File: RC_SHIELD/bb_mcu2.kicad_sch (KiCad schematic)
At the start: 14 parts, among them J1 SWD, J2 P3a, SW301 SW_Push, U1 STM32F030K6Tx, Y1 8MHz

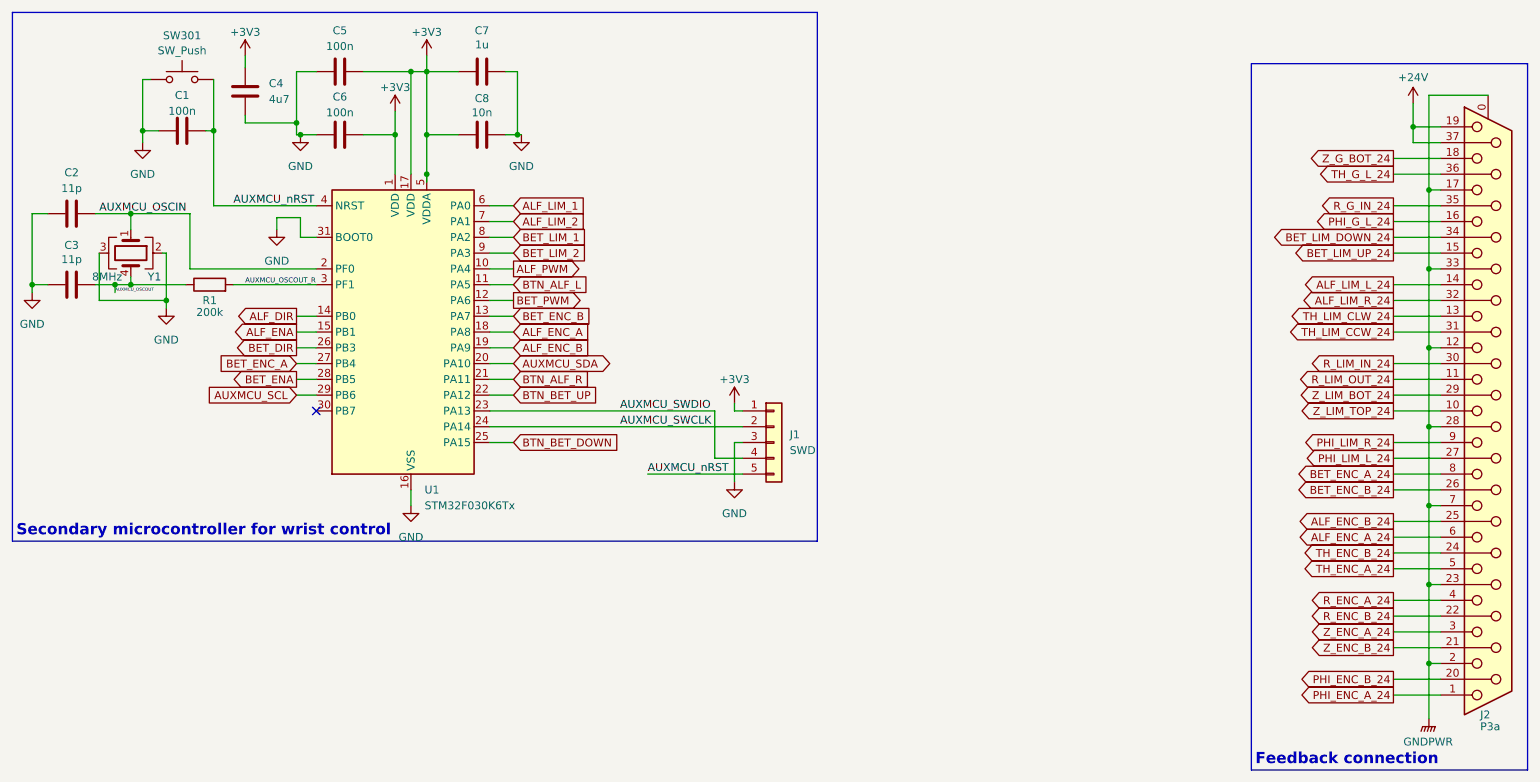
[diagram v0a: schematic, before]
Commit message: Revert "[SCH] reannotated entire schematic so PCBnew wont complain"
This reverts commit df148950bb8496d2d5af5a937770664cb0004a0d.
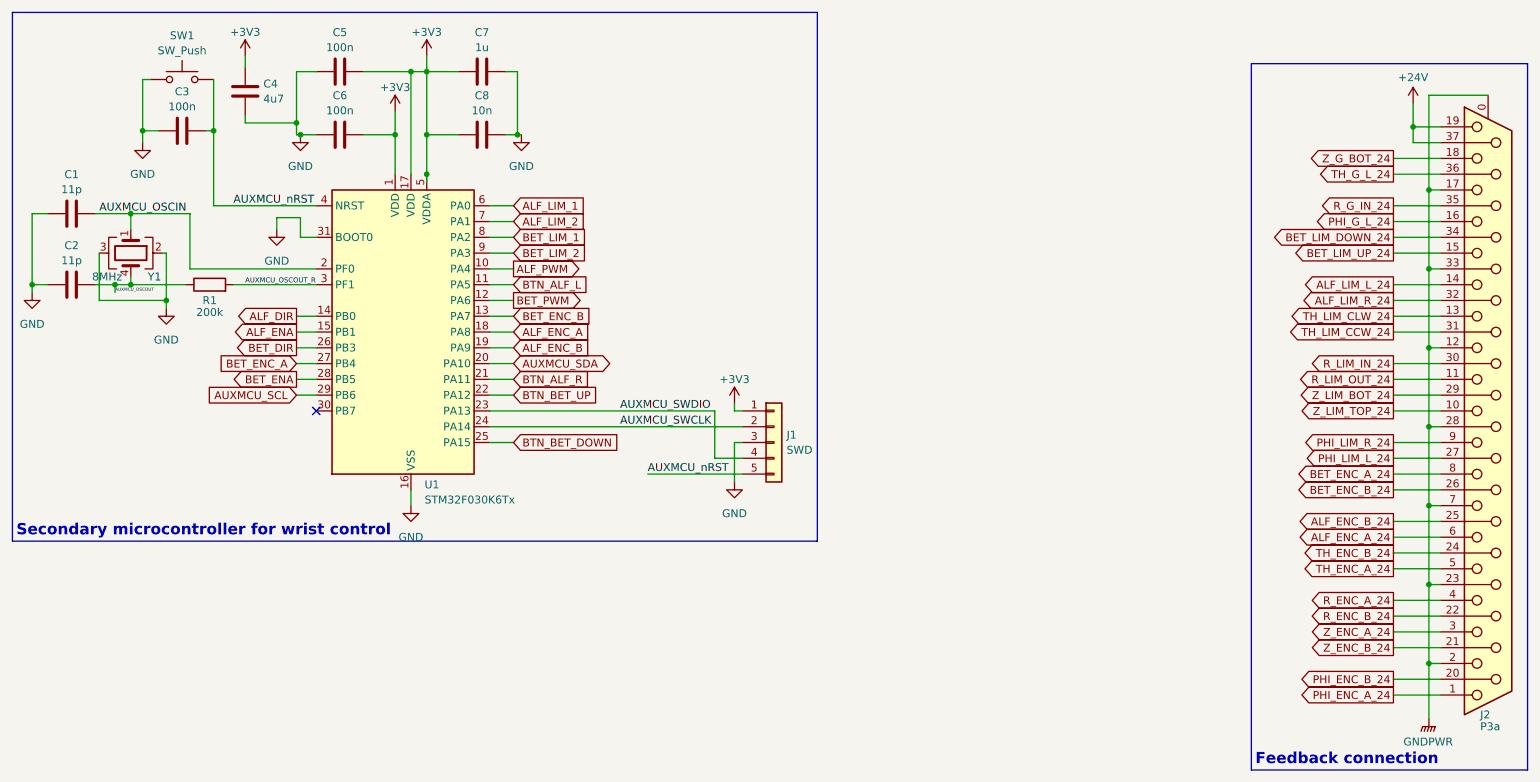
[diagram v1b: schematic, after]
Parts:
- renumbered C2 to C1, C3 to C2, C1 to C3, SW301 to SW1

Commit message: [SCH] reannotated entire schematic so PCBnew wont complain
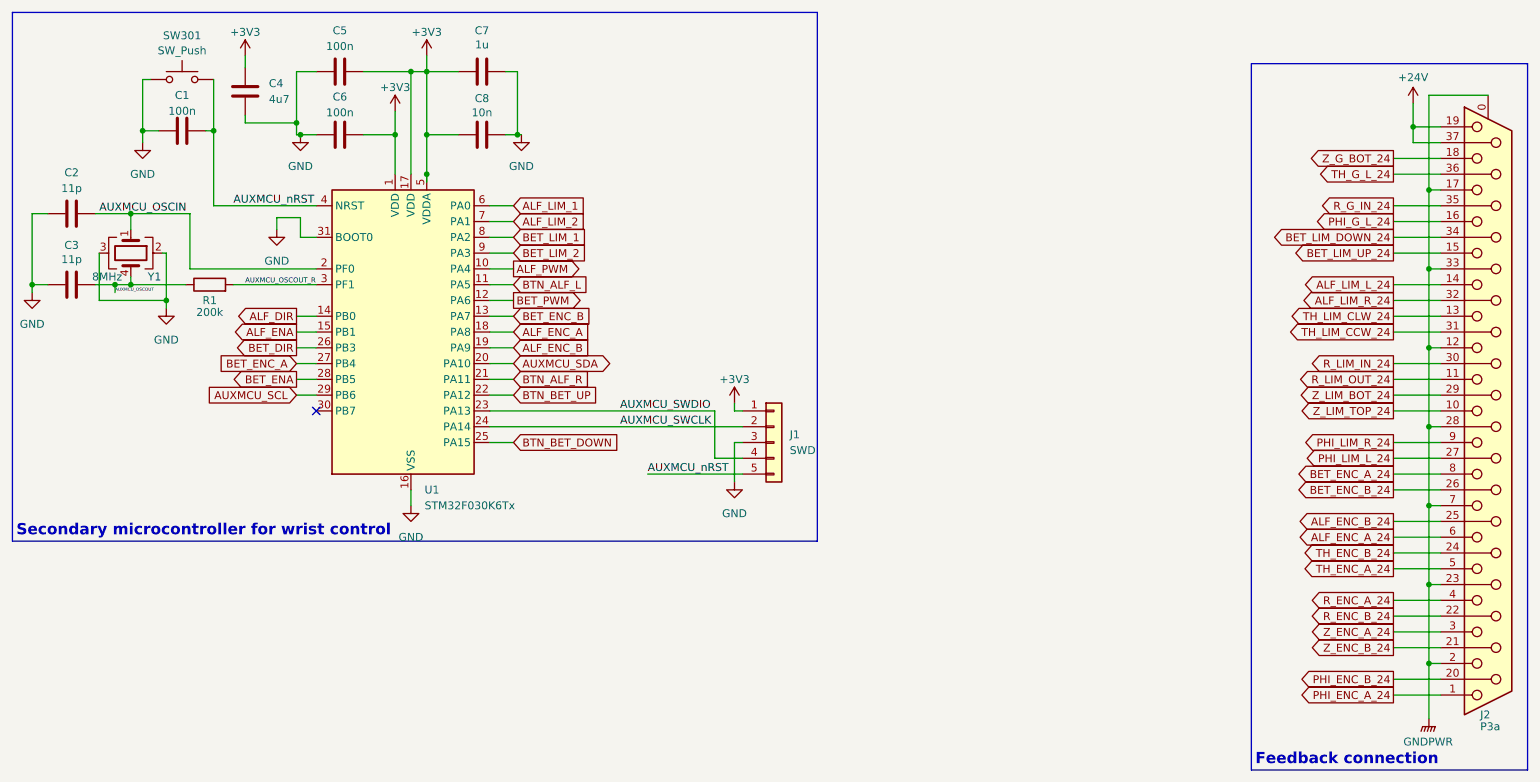
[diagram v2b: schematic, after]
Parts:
- renumbered C3 to C1, C1 to C2, C2 to C3, SW1 to SW301
